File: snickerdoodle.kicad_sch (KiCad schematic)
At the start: 11 parts, among them J2 TFM-115-01-F-D-A, J3 TFM-120-01-F-D-A, U601 TCA9800

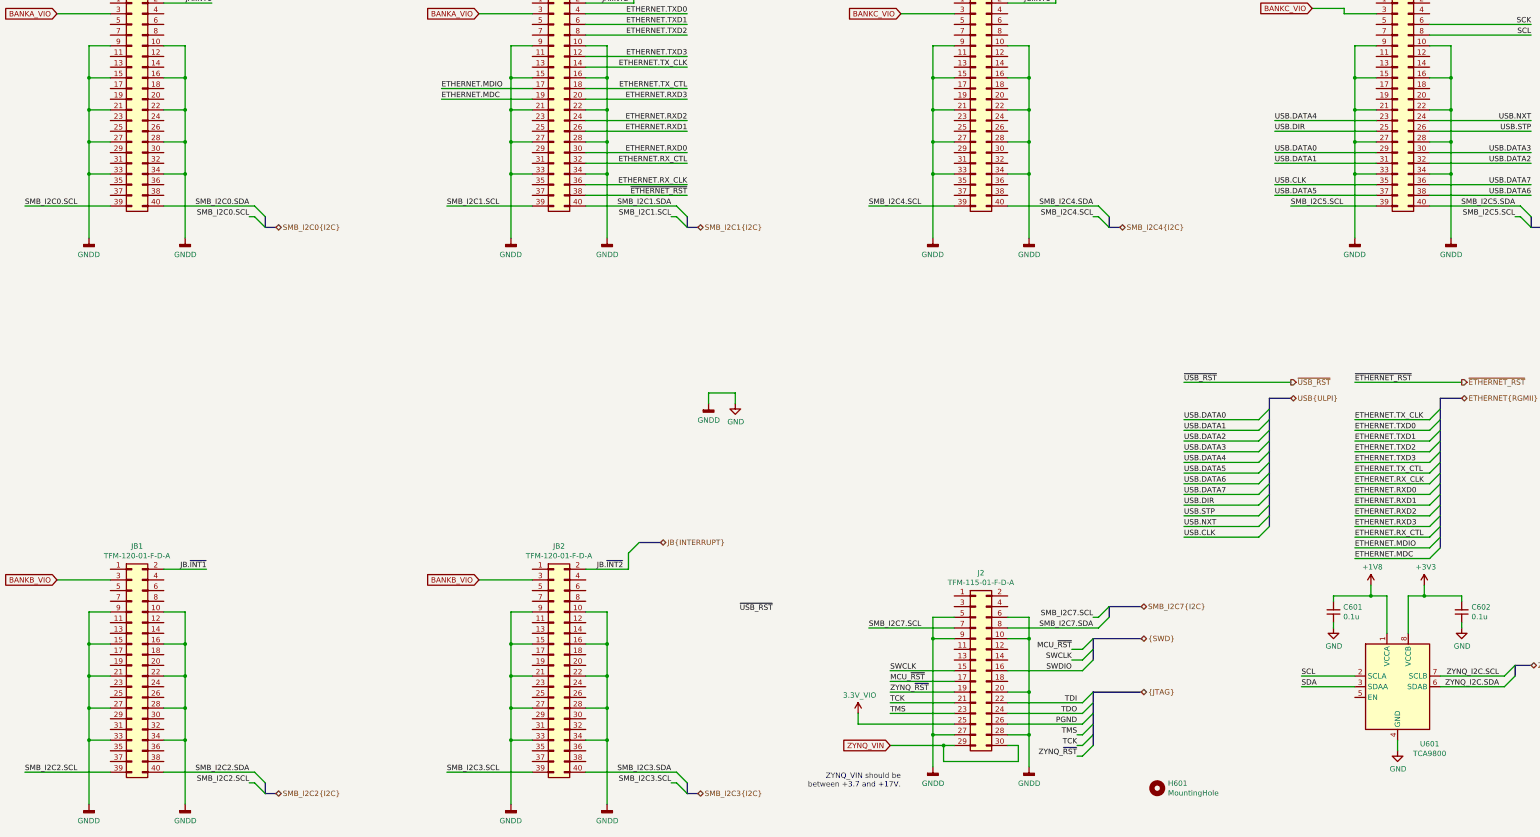
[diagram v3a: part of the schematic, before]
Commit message: Attach ethernet to PL, layout and route
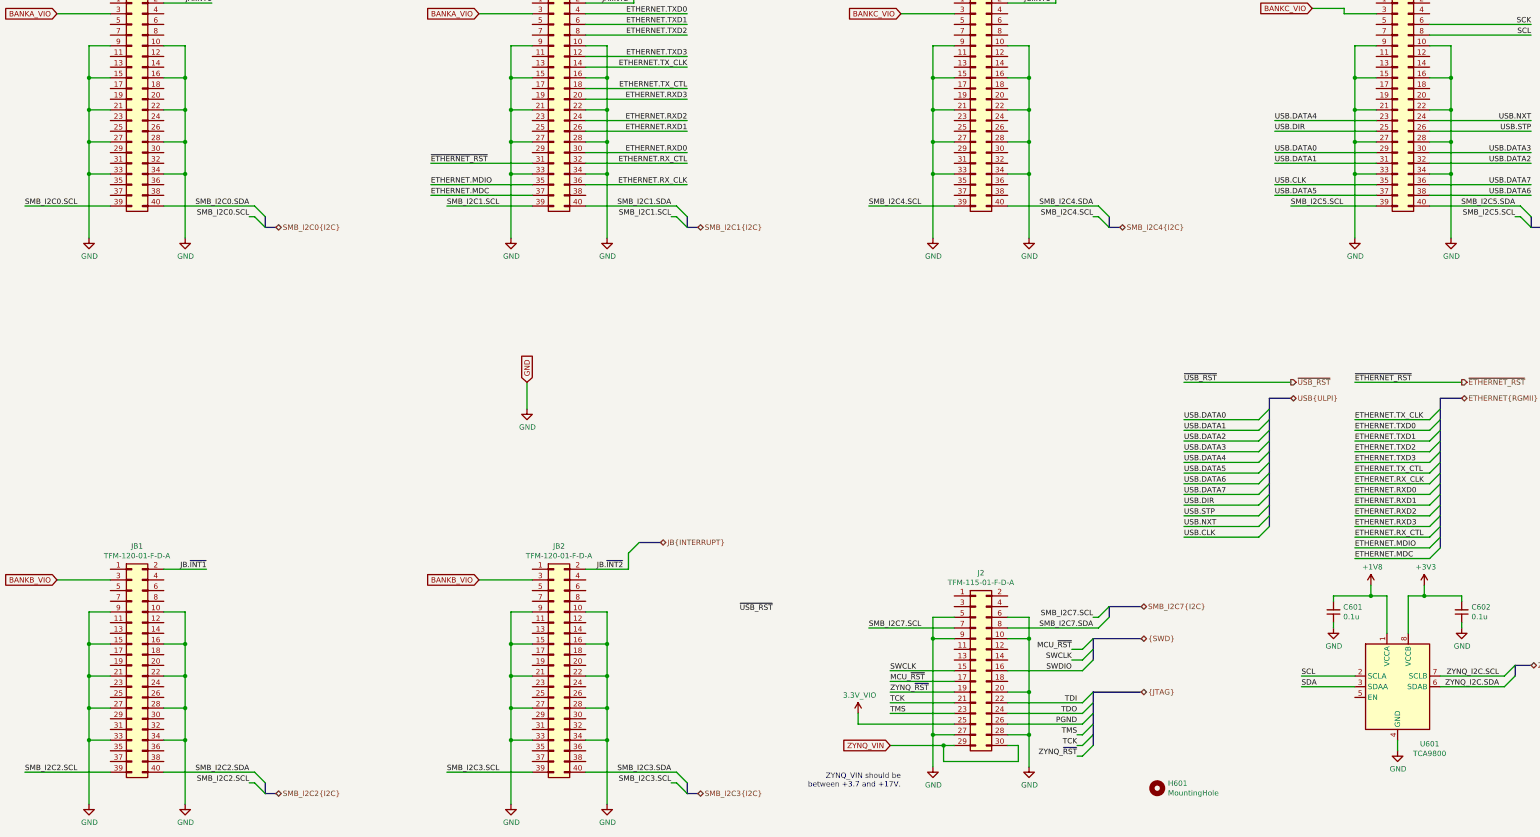
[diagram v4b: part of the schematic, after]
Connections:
- net ETHERNET.MDC: now also JA2.37 (Pin_37); no longer JA2.19 (Pin_19)
- net ETHERNET.MDIO: now also JA2.35 (Pin_35); no longer JA2.17 (Pin_17)
- net ~ETHERNET_RST: now also JA2.31 (Pin_31); no longer JA2.38 (Pin_38)

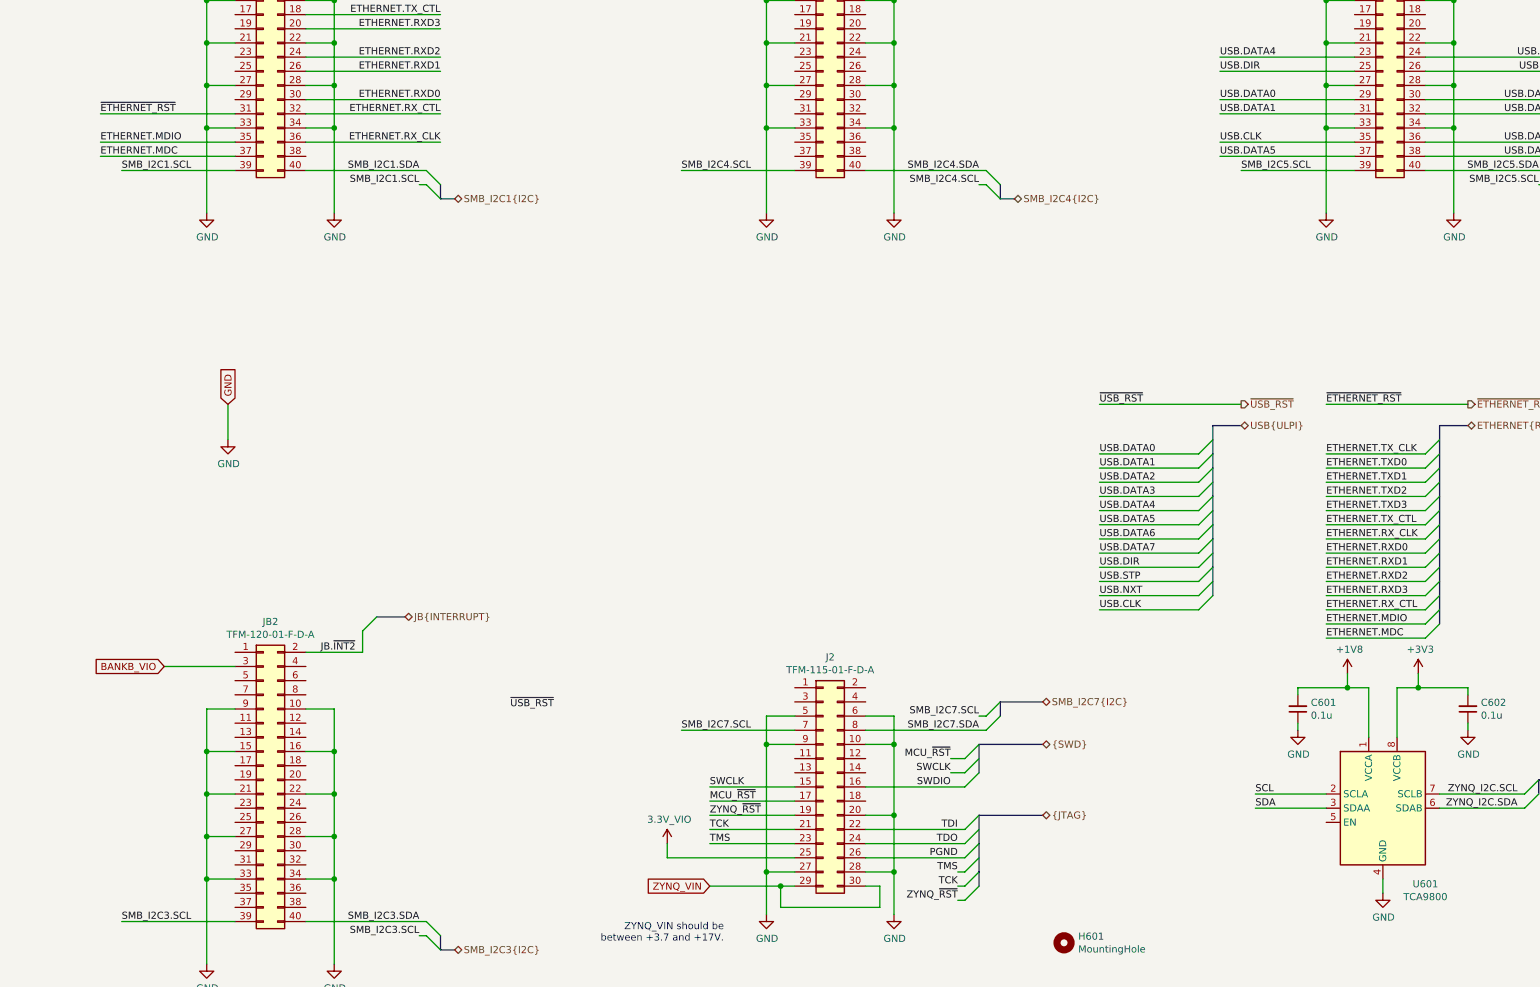
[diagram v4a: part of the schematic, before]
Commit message: Move Ethernet around to save space
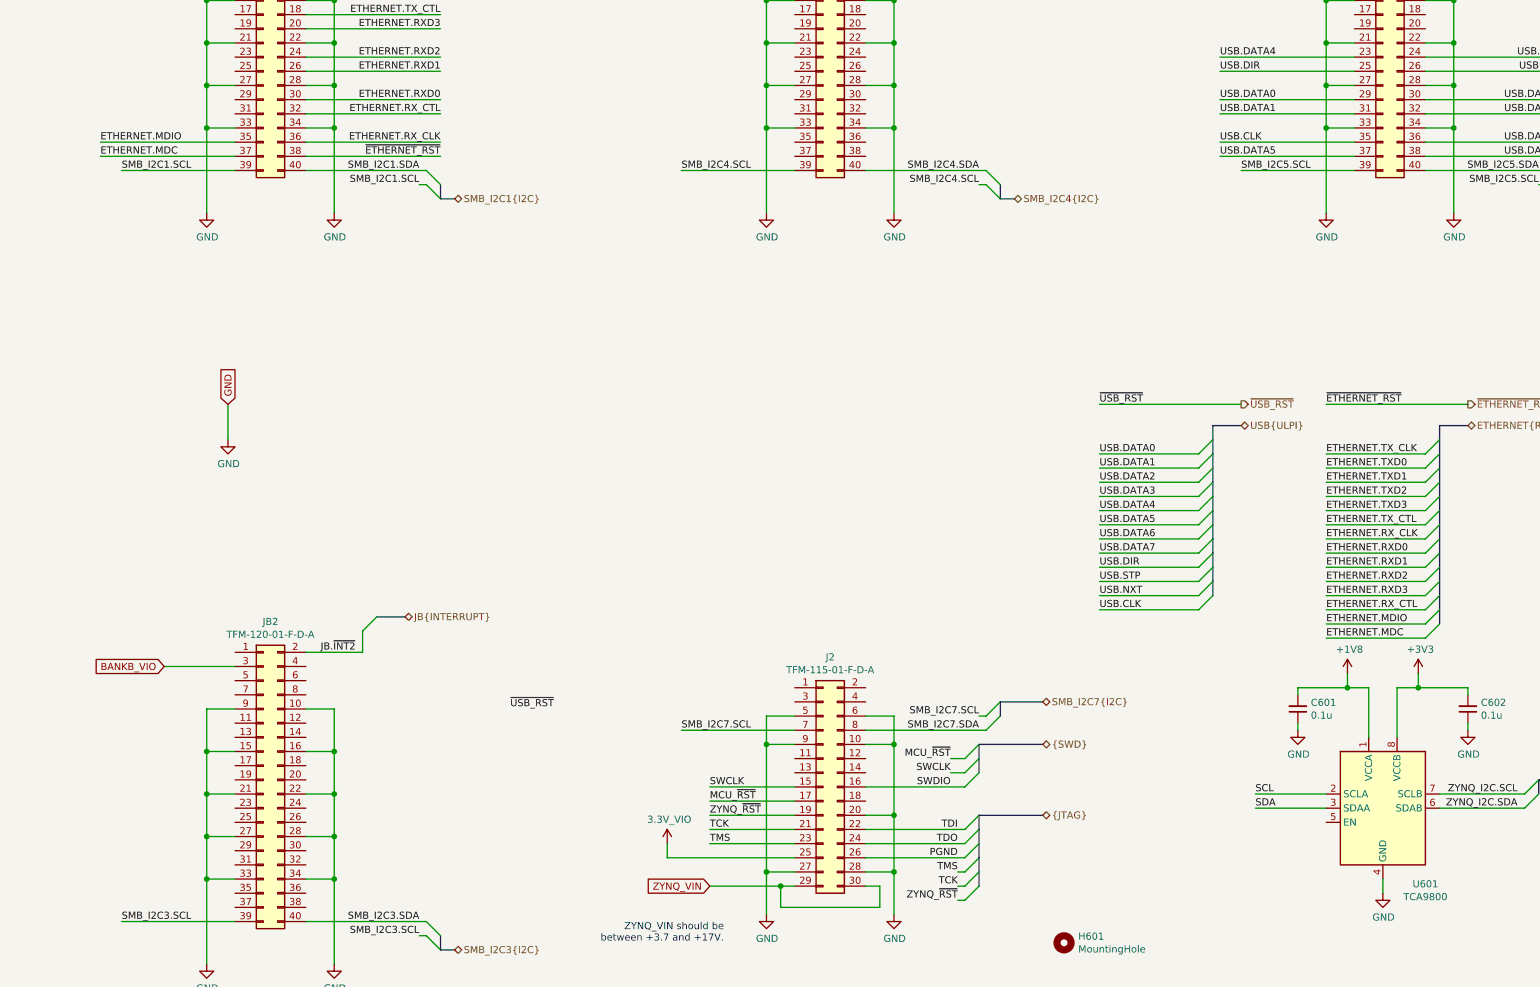
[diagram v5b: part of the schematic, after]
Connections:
- net ~ETHERNET_RST: now also JA2.38 (Pin_38); no longer JA2.31 (Pin_31)
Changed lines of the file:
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@@
-(kicad_sch (version 20200714) (host eeschema "5.99.0-unknown-a146cd9~102~ubuntu20.04.1")
+(kicad_sch (version 20200714) (host eeschema "5.99.0-unknown-9b6ade6b1~102~ubuntu20.04.1")
   (page 6 15)
   (paper "B")
@@
     (stroke (width 0) (type solid) (color 0 0 0 0))
   )
-  (wire (pts (xy 153.67 66.04) (xy 129.54 66.04))
-    (stroke (width 0) (type solid) (color 0 0 0 0))
-  )
   (wire (pts (xy 153.67 68.58) (xy 148.59 68.58))
     (stroke (width 0) (type solid) (color 0 0 0 0))
@@
     (stroke (width 0) (type solid) (color 0 0 0 0))
   )
+  (wire (pts (xy 166.37 73.66) (xy 190.5 73.66))
+    (stroke (width 0) (type solid) (color 0 0 0 0))
+  )
   (wire (pts (xy 166.37 76.2) (xy 187.96 76.2))
     (stroke (width 0) (type solid) (color 0 0 0 0))
@@
     (stroke (width 0) (type solid) (color 0 0 0 0))
   )
-  (bus (pts (xy 287.02 191.77) (xy 287.02 196.85))
+  (bus (pts (xy 287.02 191.77) (xy 287.02 194.31))
     (stroke (width 0) (type solid) (color 0 0 0 0))
   )
@@
     (stroke (width 0) (type solid) (color 0 0 0 0))
   )
-  (bus (pts (xy 287.02 196.85) (xy 287.02 201.93))
-    (stroke (width 0) (type solid) (color 0 0 0 0))
-  )
-  (bus (pts (xy 287.02 201.93) (xy 287.02 204.47))
+  (bus (pts (xy 287.02 194.31) (xy 287.02 199.39))
+    (stroke (width 0) (type solid) (color 0 0 0 0))
+  )
+  (bus (pts (xy 287.02 199.39) (xy 287.02 204.47))
     (stroke (width 0) (type solid) (color 0 0 0 0))
   )
@@
     (stroke (width 0) (type solid) (color 0 0 0 0))
   )
-  (bus (pts (xy 328.93 127) (xy 328.93 129.54))
-    (stroke (width 0) (type solid) (color 0 0 0 0))
-  )
-  (bus (pts (xy 328.93 129.54) (xy 328.93 134.62))
-    (stroke (width 0) (type solid) (color 0 0 0 0))
-  )
-  (bus (pts (xy 328.93 134.62) (xy 328.93 139.7))
-    (stroke (width 0) (type solid) (color 0 0 0 0))
-  )
-  (bus (pts (xy 328.93 139.7) (xy 328.93 142.24))
-    (stroke (width 0) (type solid) (color 0 0 0 0))
-  )
-  (bus (pts (xy 328.93 142.24) (xy 328.93 147.32))
-    (stroke (width 0) (type solid) (color 0 0 0 0))
-  )
-  (bus (pts (xy 328.93 147.32) (xy 328.93 152.4))
+  (bus (pts (xy 328.93 127) (xy 328.93 132.08))
+    (stroke (width 0) (type solid) (color 0 0 0 0))
+  )
+  (bus (pts (xy 328.93 132.08) (xy 328.93 137.16))
+    (stroke (width 0) (type solid) (color 0 0 0 0))
+  )
+  (bus (pts (xy 328.93 137.16) (xy 328.93 142.24))
+    (stroke (width 0) (type solid) (color 0 0 0 0))
+  )
+  (bus (pts (xy 328.93 142.24) (xy 328.93 144.78))
+    (stroke (width 0) (type solid) (color 0 0 0 0))
+  )
+  (bus (pts (xy 328.93 144.78) (xy 328.93 149.86))
+    (stroke (width 0) (type solid) (color 0 0 0 0))
+  )
+  (bus (pts (xy 328.93 149.86) (xy 328.93 152.4))
     (stroke (width 0) (type solid) (color 0 0 0 0))
   )
@@
     (stroke (width 0) (type solid) (color 0 0 0 0))
   )
-  (bus (pts (xy 369.57 139.7) (xy 369.57 144.78))
-    (stroke (width 0) (type solid) (color 0 0 0 0))
-  )
-  (bus (pts (xy 369.57 144.78) (xy 369.57 149.86))
-    (stroke (width 0) (type solid) (color 0 0 0 0))
-  )
-  (bus (pts (xy 369.57 149.86) (xy 369.57 154.94))
-    (stroke (width 0) (type solid) (color 0 0 0 0))
-  )
-  (bus (pts (xy 369.57 154.94) (xy 369.57 157.48))
+  (bus (pts (xy 369.57 139.7) (xy 369.57 142.24))
+    (stroke (width 0) (type solid) (color 0 0 0 0))
+  )
+  (bus (pts (xy 369.57 142.24) (xy 369.57 147.32))
+    (stroke (width 0) (type solid) (color 0 0 0 0))
+  )
+  (bus (pts (xy 369.57 147.32) (xy 369.57 152.4))
+    (stroke (width 0) (type solid) (color 0 0 0 0))
+  )
+  (bus (pts (xy 369.57 152.4) (xy 369.57 157.48))
     (stroke (width 0) (type solid) (color 0 0 0 0))
   )
@@
     (effects (font (size 1.27 1.27)) (justify right bottom))
   )
-  (label "~ETHERNET_RST" (at 129.54 66.04 0)
-    (effects (font (size 1.27 1.27)) (justify left bottom))
-  )
   (label "ETHERNET.MDIO" (at 129.54 71.12 0)
     (effects (font (size 1.27 1.27)) (justify left bottom))
@@
     (effects (font (size 1.27 1.27)) (justify right bottom))
   )
+  (label "~ETHERNET_RST" (at 190.5 73.66 180)
+    (effects (font (size 1.27 1.27)) (justify right bottom))
+  )
